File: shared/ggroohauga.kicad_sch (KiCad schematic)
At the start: 11 parts

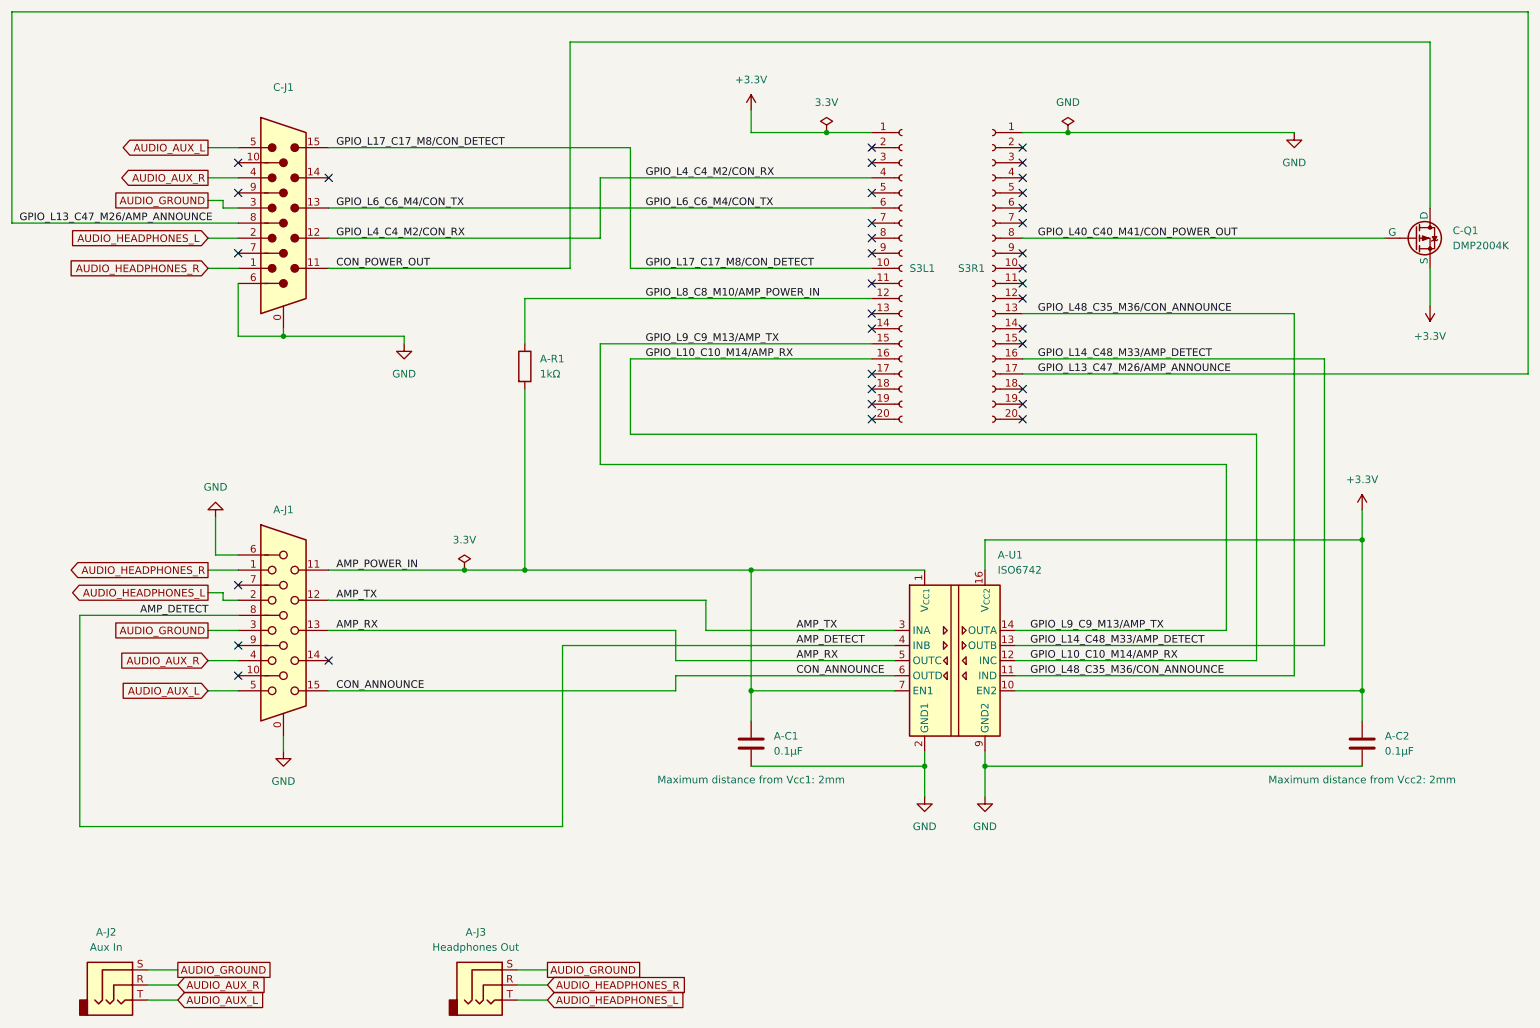
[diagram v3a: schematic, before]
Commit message: Add 4ch digital isolator and 2 TRS jacks to the amplifier PCB
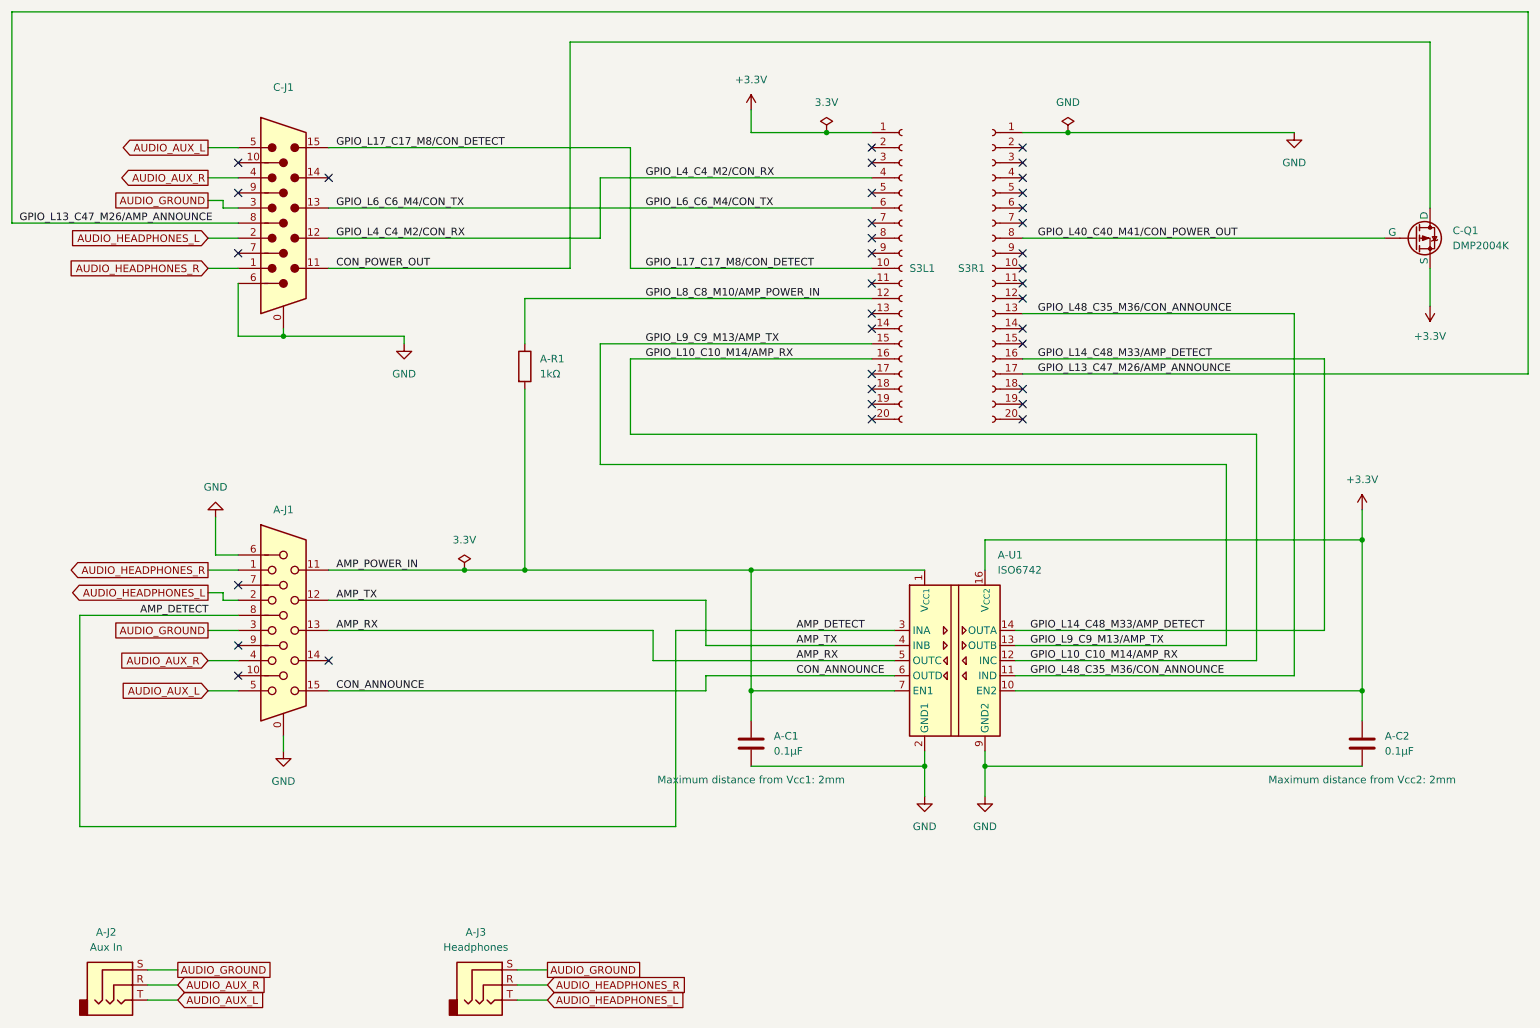
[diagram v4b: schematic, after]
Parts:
- A-J2: footprint Connector_Audio:Jack_3.5mm_CUI_SJ1-3523N_Horizontal -> ggroohauga:Jack_3.5mm_CUI_SJ1-3523N_Horizontal
- A-J3: value Headphones Out -> Headphones; footprint Connector_Audio:Jack_3.5mm_CUI_SJ1-3523N_Horizontal -> ggroohauga:Jack_3.5mm_CUI_SJ1-3523N_Horizontal
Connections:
- net AMP_DETECT: now also A-U1.3 (INA); no longer A-U1.4 (INB)
- net AMP_TX: now also A-U1.4 (INB); no longer A-U1.3 (INA)
- net GPIO_L14_C48_M33/AMP_DETECT: now also A-U1.14 (OUTA); no longer A-U1.13 (OUTB)
- net GPIO_L9_C9_M13/AMP_TX: now also A-U1.13 (OUTB); no longer A-U1.14 (OUTA)
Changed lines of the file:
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@@
-	(wire
-		(pts
-			(xy 189.23 127) (xy 241.3 127)
-		)
-		(stroke
-			(width 0)
-			(type default)
-		)
-	)
 	(wire
 		(pts
@@
 	(wire
 		(pts
+			(xy 189.23 127) (xy 224.79 127)
+		)
+		(stroke
+			(width 0)
+			(type default)
+		)
+	)
+	(wire
+		(pts
 			(xy 106.68 114.3) (xy 144.78 114.3)
 		)
@@
 	(wire
 		(pts
-			(xy 73.66 134.62) (xy 132.08 134.62)
+			(xy 73.66 134.62) (xy 137.16 134.62)
 		)
 		(stroke
@@
 	(wire
 		(pts
-			(xy 132.08 134.62) (xy 132.08 132.08)
+			(xy 137.16 134.62) (xy 137.16 132.08)
 		)
 		(stroke
@@
 	(wire
 		(pts
-			(xy 224.79 124.46) (xy 224.79 96.52)
+			(xy 224.79 96.52) (xy 224.79 127)
 		)
 		(stroke
@@
 	(wire
 		(pts
+			(xy 189.23 124.46) (xy 241.3 124.46)
+		)
+		(stroke
+			(width 0)
+			(type default)
+		)
+	)
+	(wire
+		(pts
 			(xy 105.41 186.69) (xy 110.49 186.69)
 		)
@@
 	(wire
 		(pts
-			(xy 241.3 78.74) (xy 241.3 127)
+			(xy 241.3 78.74) (xy 241.3 124.46)
 		)
 		(stroke
@@
 	(wire
 		(pts
-			(xy 73.66 124.46) (xy 132.08 124.46)
+			(xy 73.66 124.46) (xy 128.27 124.46)
 		)
 		(stroke
@@
 	(wire
 		(pts
-			(xy 137.16 119.38) (xy 137.16 124.46)
-		)
-		(stroke
-			(width 0)
-			(type default)
-		)
-	)
-	(wire
-		(pts
 			(xy 66.04 142.24) (xy 66.04 144.78)
 		)
@@
 	(wire
 		(pts
-			(xy 132.08 124.46) (xy 132.08 129.54)
-		)
-		(stroke
-			(width 0)
-			(type default)
-		)
-	)
-	(wire
-		(pts
-			(xy 132.08 132.08) (xy 168.91 132.08)
+			(xy 132.08 124.46) (xy 168.91 124.46)
+		)
+		(stroke
+			(width 0)
+			(type default)
+		)
+	)
+	(wire
+		(pts
+			(xy 128.27 124.46) (xy 128.27 129.54)
+		)
+		(stroke
+			(width 0)
+			(type default)
+		)
+	)
+	(wire
+		(pts
+			(xy 137.16 132.08) (xy 168.91 132.08)
 		)
 		(stroke
@@
 	(wire
 		(pts
-			(xy 113.03 127) (xy 168.91 127)
-		)
-		(stroke
-			(width 0)
-			(type default)
-		)
-	)
-	(wire
-		(pts
 			(xy 58.42 121.92) (xy 31.75 121.92)
 		)
@@
 	(wire
 		(pts
-			(xy 189.23 124.46) (xy 224.79 124.46)
-		)
-		(stroke
-			(width 0)
-			(type default)
-		)
-	)
-	(wire
-		(pts
 			(xy 259.08 25.4) (xy 114.3 25.4)
 		)
@@
 	(wire
 		(pts
+			(xy 137.16 119.38) (xy 137.16 127)
+		)
+		(stroke
+			(width 0)
+			(type default)
+		)
+	)
+	(wire
+		(pts
 			(xy 66.04 74.93) (xy 86.36 74.93)
 		)
@@
 	(wire
 		(pts
-			(xy 31.75 157.48) (xy 113.03 157.48)
-		)
-		(stroke
-			(width 0)
-			(type default)
-		)
-	)
-	(wire
-		(pts
-			(xy 132.08 129.54) (xy 168.91 129.54)
+			(xy 31.75 157.48) (xy 132.08 157.48)
+		)
+		(stroke
+			(width 0)
+			(type default)
+		)
+	)
+	(wire
+		(pts
+			(xy 128.27 129.54) (xy 168.91 129.54)
 		)
 		(stroke
@@
 	(wire
 		(pts
-			(xy 137.16 124.46) (xy 168.91 124.46)
-		)
-		(stroke
-			(width 0)
-			(type default)
-		)
-	)
-	(wire
-		(pts
 			(xy 124.46 63.5) (xy 165.1 63.5)
 		)
@@
 	(wire
 		(pts
-			(xy 113.03 157.48) (xy 113.03 127)
+			(xy 132.08 124.46) (xy 132.08 157.48)
 		)
 		(stroke
@@
 		(pts
 			(xy 236.22 71.12) (xy 236.22 132.08)
+		)
+		(stroke
+			(width 0)
+			(type default)
+		)
+	)
+	(wire
+		(pts
+			(xy 137.16 127) (xy 168.91 127)
 		)
 		(stroke
@@
 		)
 	)
-	(label "GPIO_L9_C9_M13{slash}AMP_TX"
-		(at 191.77 124.46 0)
-		(effects
-			(font
-				(size 1.27 1.27)
-			)
-			(justify left bottom)
-		)
-	)
 	(label "GPIO_L4_C4_M2{slash}CON_RX"
 		(at 74.93 58.42 0)
@@
 		)
 	)
+	(label "AMP_TX"
+		(at 152.4 127 0)
+		(effects
+			(font
+				(size 1.27 1.27)
+			)
+			(justify left bottom)
+		)
+	)
 	(label "AMP_RX"
 		(at 152.4 129.54 0)
@@
 		)
 	)
-	(label "AMP_TX"
+	(label "AMP_DETECT"
 		(at 152.4 124.46 0)
 		(effects
@@
 		)
 	)
-	(label "AMP_DETECT"
-		(at 152.4 127 0)
-		(effects
-			(font
-				(size 1.27 1.27)
-			)
-			(justify left bottom)
-		)
-	)
 	(label "GPIO_L17_C17_M8{slash}CON_DETECT"
 		(at 127 63.5 0)
@@
 	)
 	(label "GPIO_L14_C48_M33{slash}AMP_DETECT"
+		(at 191.77 124.46 0)
+		(effects
+			(font
+				(size 1.27 1.27)
+			)
+			(justify left bottom)
+		)
+	)
+	(label "GPIO_L9_C9_M13{slash}AMP_TX"
 		(at 191.77 127 0)
 		(effects
@@
 			)
 		)
-		(property "Footprint" "Connector_Audio:Jack_3.5mm_CUI_SJ1-3523N_Horizontal"
+		(property "Footprint" "ggroohauga:Jack_3.5mm_CUI_SJ1-3523N_Horizontal"
 			(at 38.1 184.15 0)
 			(effects
@@
 			)
 		)
-		(property "Value" "Headphones Out"
+		(property "Value" "Headphones"
 			(at 98.425 177.8 0)
 			(effects
@@
 			)
 		)
-		(property "Footprint" "Connector_Audio:Jack_3.5mm_CUI_SJ1-3523N_Horizontal"
+		(property "Footprint" "ggroohauga:Jack_3.5mm_CUI_SJ1-3523N_Horizontal"
 			(at 100.33 184.15 0)
 			(effects
